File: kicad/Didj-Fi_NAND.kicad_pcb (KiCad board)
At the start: 2 copper layers, 44.9 x 33.5 mm, 23 parts, among them J1 didj_cart, J2 Conn_01x04_Male, U1 NAND-8BIT, U2 ESP-12F

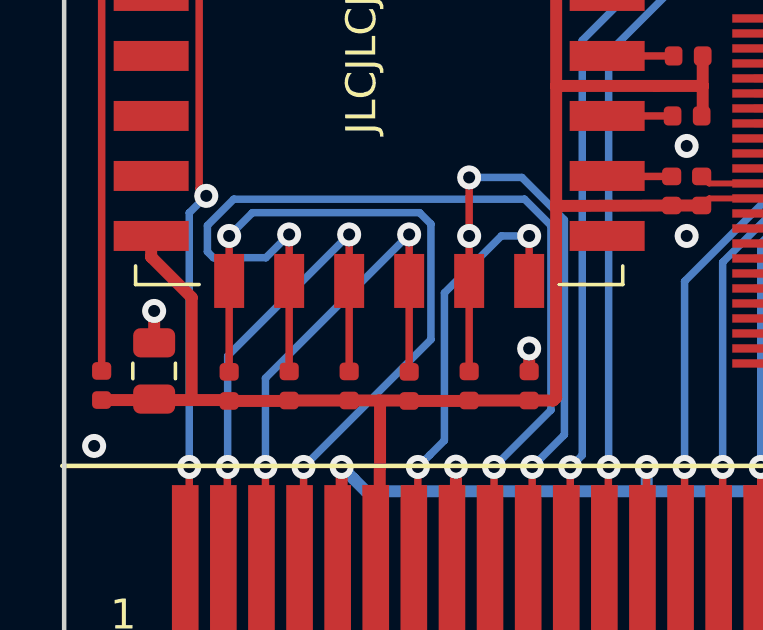
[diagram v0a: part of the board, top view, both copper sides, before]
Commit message: minor tweaks
removed an extra via
re-routed a couple of traces
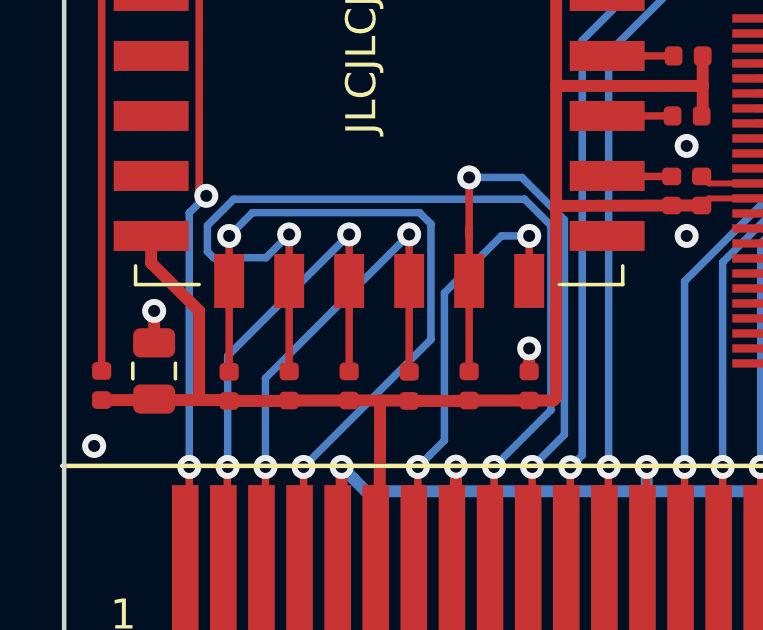
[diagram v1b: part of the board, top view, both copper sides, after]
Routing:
- net /DAT1: vias 3 -> 2
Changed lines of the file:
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@@
   (segment (start 127.75 112.884998) (end 128.75 112.884998) (width 0.4) (layer F.Cu) (net 1))
   (segment (start 128.75 112.884998) (end 129.735 112.884998) (width 0.4) (layer F.Cu) (net 1))
-  (segment (start 122.5 112.869998) (end 123.72 112.869998) (width 0.4) (layer F.Cu) (net 1))
   (segment (start 138.5 106.384998) (end 139.5 106.384998) (width 0.4) (layer F.Cu) (net 1))
   (segment (start 138.5 106.384998) (end 134.650001 106.399998) (width 0.4) (layer F.Cu) (net 1))
@@
   (segment (start 139.535 101.399998) (end 139.535 102.399998) (width 0.4) (layer F.Cu) (net 1))
   (segment (start 119.5 112.869998) (end 122.5 112.869998) (width 0.4) (layer F.Cu) (net 1))
-  (segment (start 121.15 107.399998) (end 121.15 108.099998) (width 0.4) (layer F.Cu) (net 1))
-  (segment (start 121.15 108.099998) (end 122.5 109.449998) (width 0.4) (layer F.Cu) (net 1))
-  (segment (start 122.5 109.449998) (end 122.5 112.869998) (width 0.4) (layer F.Cu) (net 1))
+  (segment (start 122.75 109.899998) (end 122.75 112.869998) (width 0.4) (layer F.Cu) (net 1))
+  (segment (start 121.15 108.299998) (end 122.75 109.899998) (width 0.4) (layer F.Cu) (net 1))
+  (segment (start 121.15 107.399998) (end 121.15 108.299998) (width 0.4) (layer F.Cu) (net 1))
+  (segment (start 122.5 112.869998) (end 122.75 112.869998) (width 0.4) (layer F.Cu) (net 1))
+  (segment (start 122.75 112.869998) (end 123.72 112.869998) (width 0.4) (layer F.Cu) (net 1))
   (via (at 127.5 115.099998) (size 0.8) (drill 0.4) (layers F.Cu B.Cu) (net 2))
   (segment (start 127.5 120.149498) (end 127.5 115.099998) (width 0.4) (layer F.Cu) (net 2))
@@
   (segment (start 133.85 120.149498) (end 133.85 115.099998) (width 0.25) (layer F.Cu) (net 3))
   (segment (start 131.75 111.914998) (end 131.75 108.899998) (width 0.25) (layer F.Cu) (net 3))
-  (via (at 131.75 107.399998) (size 0.8) (drill 0.4) (layers F.Cu B.Cu) (net 3))
   (segment (start 131.75 107.149998) (end 131.75 108.899998) (width 0.25) (layer F.Cu) (net 3))
   (segment (start 133.509401 105.449987) (end 131.75 105.449987) (width 0.25) (layer B.Cu) (net 3))

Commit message: silk screen changes
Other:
- board text added: "0"
- board text added: "1"
- board text added: "3.3v"
- board text added: "7 6 5 | Boot mode --------------- X X X | Device default X 0 0 | UART 0 0 1 | Internal NAND 1 0 1 | Cartridge NAND X 1 1 | None (RAM)"
- board text added: "Didj-Fi NAND v1.0"
- board text added: "GND"
- board text added: "RX"
- board text added: "SD5"
- board text added: "SD6"
- board text added: "SD7"
- board text added: "TX"
- board text removed: "5"
- board text removed: "6"
- board text removed: "7"
- board text removed: "7 6 5 | Arrow = 0 ------------------- X 0 0 | UART Boot 0 0 1 | Internal NAND Boot 1 0 1 | Cartridge NAND Boot"
- board text removed: "Didj-Fi NAND"
- board text removed: "v1.0"
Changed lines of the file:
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@@
   (general
     (thickness 1.6)
-    (drawings 14)
+    (drawings 22)
     (tracks 330)
     (zones 0)
@@
     (fp_line (start 0 0) (end 0 10.8) (layer Dwgs.User) (width 0.15))
     (fp_line (start 0 0) (end 45 0) (layer F.SilkS) (width 0.15))
-    (fp_text user 1 (at 2.032 4.958) (layer F.SilkS)
-      (effects (font (size 1 1) (thickness 0.15)))
-    )
-    (fp_text user 30 (at 42.926 4.958) (layer F.SilkS)
+    (fp_text user 1 (at 2.032 4.958) (layer F.SilkS) hide
+      (effects (font (size 1 1) (thickness 0.15)))
+    )
+    (fp_text user 30 (at 42.926 4.958) (layer F.SilkS) hide
       (effects (font (size 1 1) (thickness 0.15)))
     )
@@
     )
   )
-  (gr_text v1.0 (at 146.25 96.5) (layer F.SilkS)
-    (effects (font (size 0.9 0.9) (thickness 0.15)))
-  )
-  (gr_text v1.0 (at 120.5 97) (layer B.SilkS)
-    (effects (font (size 0.9 0.9) (thickness 0.15)) (justify mirror))
-  )
-  (gr_text "7 6 5 | Arrow = 0\n-------------------\nX 0 0 | UART Boot\n0 0 1 | Internal NAND Boot\n1 0 1 | Cartridge NAND Boot" (at 161.75 120.649998) (layer B.SilkS)
-    (effects (font (size 0.9 0.9) (thickness 0.15)) (justify left mirror))
-  )
-  (gr_text "Didj-Fi NAND" (at 139.5 94.649998) (layer B.SilkS)
-    (effects (font (size 2 2) (thickness 0.4)) (justify left mirror))
-  )
-  (gr_text 5 (at 153.75 98.399998) (layer F.SilkS)
-    (effects (font (size 1 1) (thickness 0.15)))
-  )
-  (gr_text 6 (at 157.5 98.399998) (layer F.SilkS)
-    (effects (font (size 1 1) (thickness 0.15)))
-  )
-  (gr_text 7 (at 161.25 98.399998) (layer F.SilkS)
-    (effects (font (size 1 1) (thickness 0.15)))
+  (gr_text GND (at 148.9 95.5 90) (layer F.SilkS)
+    (effects (font (size 1 1) (thickness 0.2)) (justify right))
+  )
+  (gr_text 3.3v (at 146.25 95.5 90) (layer F.SilkS)
+    (effects (font (size 1 1) (thickness 0.2)) (justify right))
+  )
+  (gr_text TX (at 143.75 95.5 90) (layer F.SilkS)
+    (effects (font (size 1 1) (thickness 0.2)) (justify right))
+  )
+  (gr_text RX (at 141.25 95.5 90) (layer F.SilkS)
+    (effects (font (size 1 1) (thickness 0.2)) (justify right))
+  )
+  (gr_text 1 (at 159.25 96.5) (layer F.SilkS)
+    (effects (font (size 0.6 0.6) (thickness 0.125)))
+  )
+  (gr_text 0 (at 159.25 94) (layer F.SilkS)
+    (effects (font (size 0.6 0.6) (thickness 0.125)))
+  )
+  (gr_text 0 (at 155.5 94) (layer F.SilkS)
+    (effects (font (size 0.6 0.6) (thickness 0.125)))
+  )
+  (gr_text 1 (at 155.5 96.5) (layer F.SilkS)
+    (effects (font (size 0.6 0.6) (thickness 0.125)))
+  )
+  (gr_text 1 (at 151.75 96.5) (layer F.SilkS)
+    (effects (font (size 0.6 0.6) (thickness 0.125)))
+  )
+  (gr_text 0 (at 151.75 94) (layer F.SilkS)
+    (effects (font (size 0.6 0.6) (thickness 0.125)))
+  )
+  (gr_text "7 6 5 | Boot mode\n---------------\nX X X | Device default\nX 0 0 | UART\n0 0 1 | Internal NAND\n1 0 1 | Cartridge NAND\nX 1 1 | None (RAM)" (at 162 120.5) (layer B.SilkS)
+    (effects (font (size 0.75 0.75) (thickness 0.15)) (justify left mirror))
+  )
+  (gr_text "Didj-Fi NAND v1.0" (at 140 94.5) (layer B.SilkS)
+    (effects (font (size 1.5 1.5) (thickness 0.3)) (justify left mirror))
+  )
+  (gr_text SD5 (at 153.75 98.25 90) (layer F.SilkS)
+    (effects (font (size 0.6 0.6) (thickness 0.125)))
+  )
+  (gr_text SD6 (at 157.5 98.25 90) (layer F.SilkS)
+    (effects (font (size 0.6 0.6) (thickness 0.125)))
+  )
+  (gr_text SD7 (at 161.25 98.25 90) (layer F.SilkS)
+    (effects (font (size 0.6 0.6) (thickness 0.125)))
   )
   (gr_text JLCJLCJLCJLC (at 128.156 99.765998 90) (layer F.SilkS)
     (effects (font (size 1 1) (thickness 0.15)))
   )
-  (gr_text jkent.net/w/didjfi (at 136.5 97.399998) (layer B.SilkS)
-    (effects (font (size 1.5 0.9) (thickness 0.15)) (justify left mirror))
-  )
-  (gr_text "Didj-Fi NAND" (at 139 98.149998) (layer F.SilkS)
+  (gr_text jkent.net/w/didjfi (at 136.25 97.25) (layer B.SilkS)
+    (effects (font (size 1.5 1) (thickness 0.15)) (justify left mirror))
+  )
+  (gr_text "Didj-Fi NAND v1.0" (at 135 113.5) (layer F.SilkS)
     (effects (font (size 1.5 1.1) (thickness 0.2)) (justify left))
   )

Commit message: prepare for manufacture
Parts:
- R9: value 4.7k -> 10k
- turned U1 to 90 degrees
